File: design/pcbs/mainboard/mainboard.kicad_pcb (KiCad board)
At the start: 4 copper layers, 150 x 130 mm, 267 parts, among them J1 Conn_Coaxial, J10 Conn_01x04, J11 Conn_01x04, J15 Conn_01x01, J16 Conn_01x01, J17 Conn_01x01, J18 Conn_01x01, J2 Conn_Coaxial, J4 AudioJackSw, J5 Conn_01x03, K1 EC2-5NU, K2 EC2-5NU, K3 EC2-12NU, K4 EC2-12NU, Q1 SS8050, Q10 SS8050, Q11 SS8050, Q12 SS8050, Q13 SS8550, Q14 SS8550, Q2 SS8050, Q3 SS8050, Q4 SS8050, Q5 SS8550, Q6 SS8550, Q7 SS8050, Q8 SS8050, Q9 SS8050, U1 TPS79318-EP, U10 TPS7A49, U11 PCM1792A, U12 OPA1612AxD, U13 OPA1612AxD, U14 OPA1612AxD, U15 CCHD-575, U16 5PB1102, U17 STM8S003F3P, U18 Combo384, U19 TPS7A49, U2 SRC4392, U20 TPS7A30, U3 TLV1117-33, U4 TPS7A49, U5 TPS7A30, U6 Si8645BA-B-IU, U7 OPA1612AxD, U8 LME49600, U9 LME49600

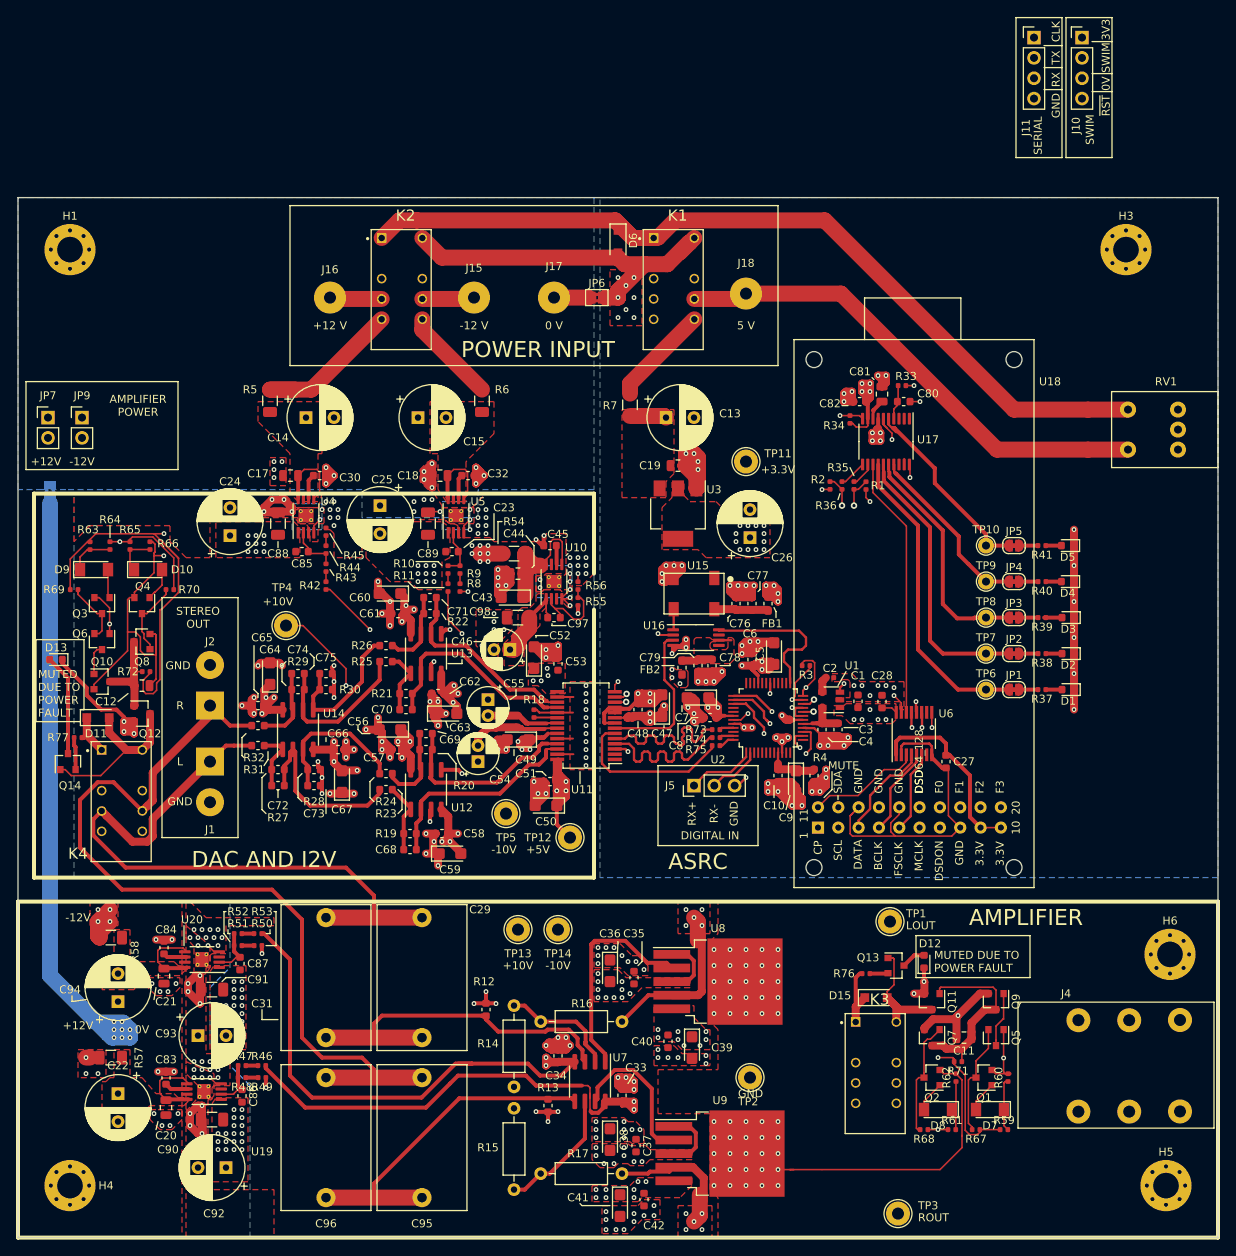
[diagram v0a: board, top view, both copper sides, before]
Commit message: Completed layout of main board, cleaned up some libraries.
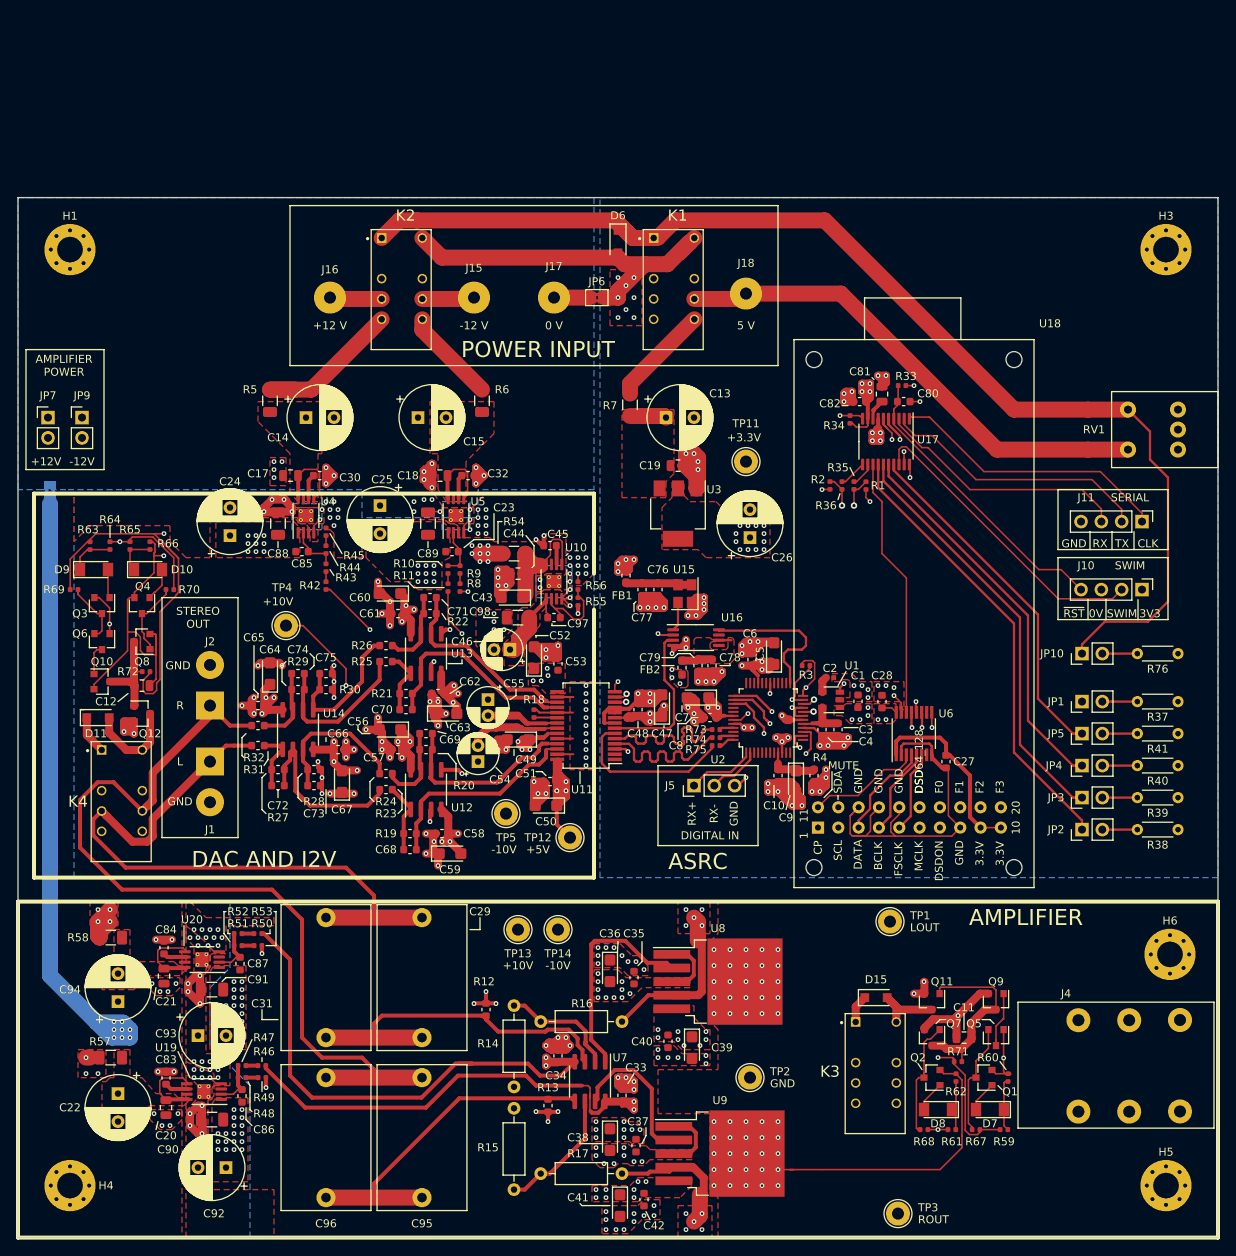
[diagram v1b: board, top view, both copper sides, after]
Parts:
- removed D1: Red, LED_SMD:LED_0603_1608Metric
- removed D12, D13: LED, LED_SMD:LED_0603_1608Metric
- removed D2: Yellow, LED_SMD:LED_0603_1608Metric
- removed D3: Green, LED_SMD:LED_0603_1608Metric
- removed D4: Blue, LED_SMD:LED_0603_1608Metric
- removed D5: White, LED_SMD:LED_0603_1608Metric
- removed Q13, Q14: SS8550, Package_TO_SOT_SMD:SOT-23
- removed R77: 1.5k, Resistor_SMD:R_0402_1005Metric
- removed TP10, TP6, TP7, TP8, TP9: ~, TestPoint:TestPoint_THTPad_D2.0mm_Drill1.0mm
- added JP10: ~, Connector_PinHeader_2.54mm:PinHeader_1x02_P2.54mm_Vertical, F.Cu at (123.0, 157.0)
- JP1, JP2, JP3, JP4, JP5: footprint Jumper:SolderJumper-2_P1.3mm_Bridged_RoundedPad1.0x1.5mm -> Connector_PinHeader_2.54mm:PinHeader_1x02_P2.54mm_Vertical
- R37, R38: value 220 -> ~; footprint Resistor_SMD:R_0402_1005Metric -> Resistor_THT:R_Axial_DIN0204_L3.6mm_D1.6mm_P5.08mm_Horizontal
- R39, R41: value 33 -> ~; footprint Resistor_SMD:R_0402_1005Metric -> Resistor_THT:R_Axial_DIN0204_L3.6mm_D1.6mm_P5.08mm_Horizontal
- R40: value 47 -> ~; footprint Resistor_SMD:R_0402_1005Metric -> Resistor_THT:R_Axial_DIN0204_L3.6mm_D1.6mm_P5.08mm_Horizontal
- R76: value 1.5k -> ~; footprint Resistor_SMD:R_0402_1005Metric -> Resistor_THT:R_Axial_DIN0204_L3.6mm_D1.6mm_P5.08mm_Horizontal
- U15: value CCHD-575 -> KC3225K24.5760C1GE00; footprint mainboard:CCHD-575 -> Crystal:Crystal_SMD_3225-4Pin_3.2x2.5mm
- moved J10 69.4 mm to (130.5, 149.0), turned to 270 degrees
- moved J11 62.0 mm to (130.5, 140.5), turned to 270 degrees
- moved R76 55.9 mm to (135.0, 157.0), turned to 180 degrees
- moved R41 29.0 mm to (135.0, 167.0)
- moved R40 28.6 mm to (135.0, 171.0)
- moved R39 28.2 mm to (135.0, 175.0)
- moved R38 27.8 mm to (135.0, 179.0)
- moved JP5 25.0 mm to (123.0, 167.0), turned to 90 degrees
- moved JP4 24.5 mm to (123.0, 171.0), turned to 90 degrees
- moved JP3 24.1 mm to (123.0, 175.0), turned to 90 degrees
- moved JP2 23.6 mm to (123.0, 179.0), turned to 90 degrees
- moved FB1 18.1 mm to (66.0, 147.2)
- moved R37 17.1 mm to (135.0, 163.0)
- moved C77 13.9 mm to (68.0, 149.0), turned to 90 degrees
- moved C76 9.91 mm to (70.0, 149.0), turned to 90 degrees
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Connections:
- JP1 pad 1: /MCU/DISP1 -> /MCU/PA1
- JP2 pad 1: /MCU/DISP2 -> /MCU/PC4
- JP3 pad 1: /MCU/DISP3 -> /MCU/PC5
- JP4 pad 1: /MCU/DISP4 -> /MCU/PC6
- JP5 pad 1: /MCU/DISP5 -> /MCU/PC7
- R37 pad 1: Net-(D1-Pad2) -> GNDD
- R38 pad 1: Net-(D2-Pad2) -> GNDD
- R39 pad 1: Net-(D3-Pad2) -> GNDD
- R40 pad 1: Net-(D4-Pad2) -> GNDD
- R41 pad 1: Net-(D5-Pad2) -> GNDD
- R76 pad 1: +10V_AMP -> GNDD
- U15 pad 1: Net-(U15-Pad1) -> GNDD
- U15 pad 2: GNDD -> Net-(C76-Pad2)
- U15 pad 3: Net-(U15-Pad3) -> Net-(C76-Pad2)
- U15 pad 4: Net-(C76-Pad2) -> Net-(U15-Pad4)
- U16 pad 1: Net-(U15-Pad3) -> Net-(U15-Pad4)
- U17 pad 14: /MCU/DISP1 -> /MCU/PC4
- U17 pad 15: /MCU/DISP2 -> /MCU/PC5
- U17 pad 16: /MCU/DISP3 -> /MCU/PC6
- U17 pad 17: /MCU/DISP4 -> /MCU/PC7
- U17 pad 5: /MCU/DISP5 -> /MCU/PA1
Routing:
- net /MCU/PC4: track 0.00 -> 56.2 mm
- net /MCU/PC5: track 0.00 -> 52.6 mm
- net /MCU/PC6: track 0.00 -> 48.3 mm
- net /MCU/PA1: track 0.00 -> 45.9 mm, vias 0 -> 1
- net /MCU/PC7: track 0.00 -> 44.1 mm
- net /PSU/POWERON: track 108.9 -> 149.1 mm
- net /MCU/DISP1: track 38.6 -> 0.00 mm
- net /MCU/SWIM: track 0.00 -> 38.2 mm
- net /MCU/DIAL: track 0.74 -> 37.0 mm, vias 0 -> 1
- net /MCU/UART_CK: track 0.00 -> 35.2 mm
- net /MCU/DISP2: track 35.0 -> 0.00 mm
- net /MCU/UART_TX: track 0.00 -> 33.8 mm
- net /MCU/NRST: track 4.36 -> 37.0 mm
- net /MCU/UART_RX: track 0.00 -> 32.0 mm
- net /MCU/DISP3: track 29.3 -> 0.00 mm
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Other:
- board text removed: "MUTED DUE TO POWER FAULT"

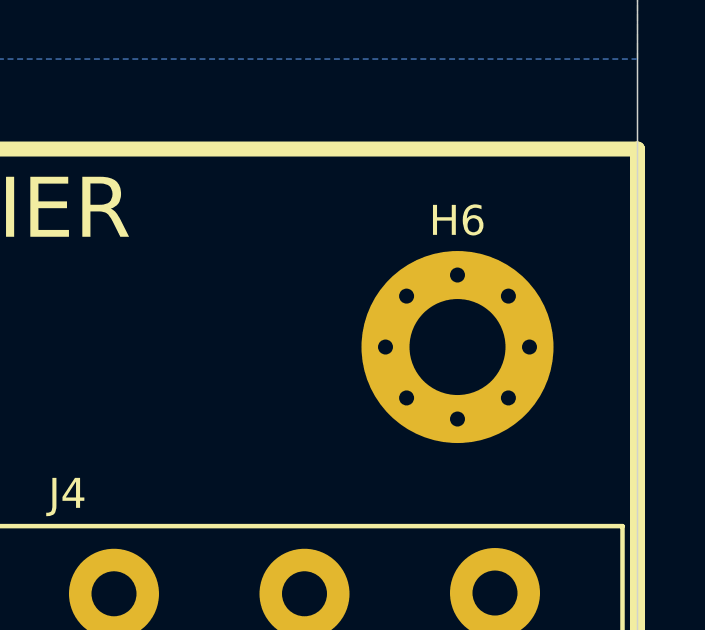
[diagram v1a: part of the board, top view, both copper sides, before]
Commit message: Fixed mounting hole alignment
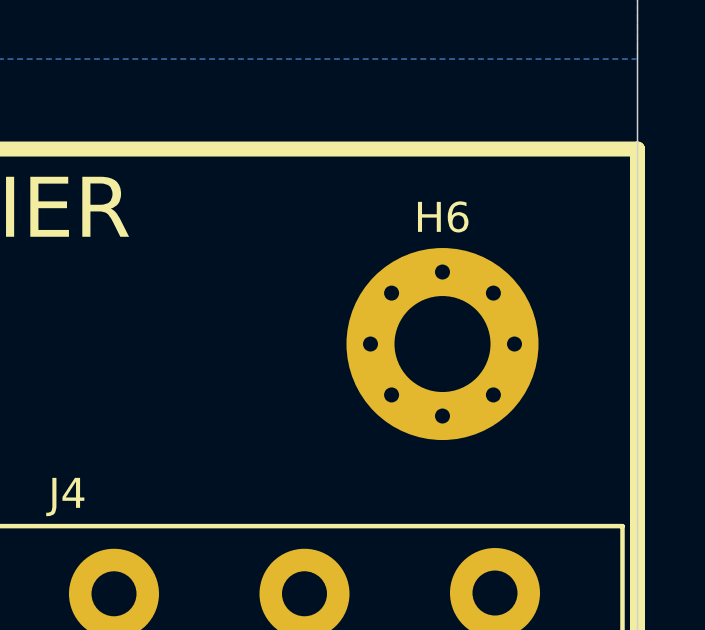
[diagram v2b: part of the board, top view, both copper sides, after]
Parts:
- moved H6 0.51 mm to (133.5, 194.5)
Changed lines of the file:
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@@
   )
   (setup
-    (last_trace_width 0.29337)
+    (last_trace_width 0.2)
     (user_trace_width 0.2)
     (user_trace_width 0.29337)
@@
   )
   (module MountingHole:MountingHole_3.2mm_M3_Pad_Via (layer F.Cu)
-    (at 134 194.6)
+    (at 133.5 194.5)
     (descr "Mounting Hole 3.2mm, M3")
     (tags "mounting hole 3.2mm m3")
@@
       (pts
         (xy 97 160.5) (xy 100.75 160.5) (xy 100.75 164) (xy 100.25 164) (xy 100.25 163)
-        (xy 97 163) (xy 97 160.5) (xy 97 160.5) (xy 97 160.5) (xy 97 160.5)
+        (xy 97 163) (xy 97 160.5)
       )
     )
@@
     (polygon
       (pts
-        (xy 99.75 165.25) (xy 99.25 165.75) (xy 97 165.75) (xy 97 163.25) (xy 97 163.25)
-        (xy 99.75 163.25)
+        (xy 99.75 165.25) (xy 99.25 165.75) (xy 97 165.75) (xy 97 163.25) (xy 99.75 163.25)
       )
     )

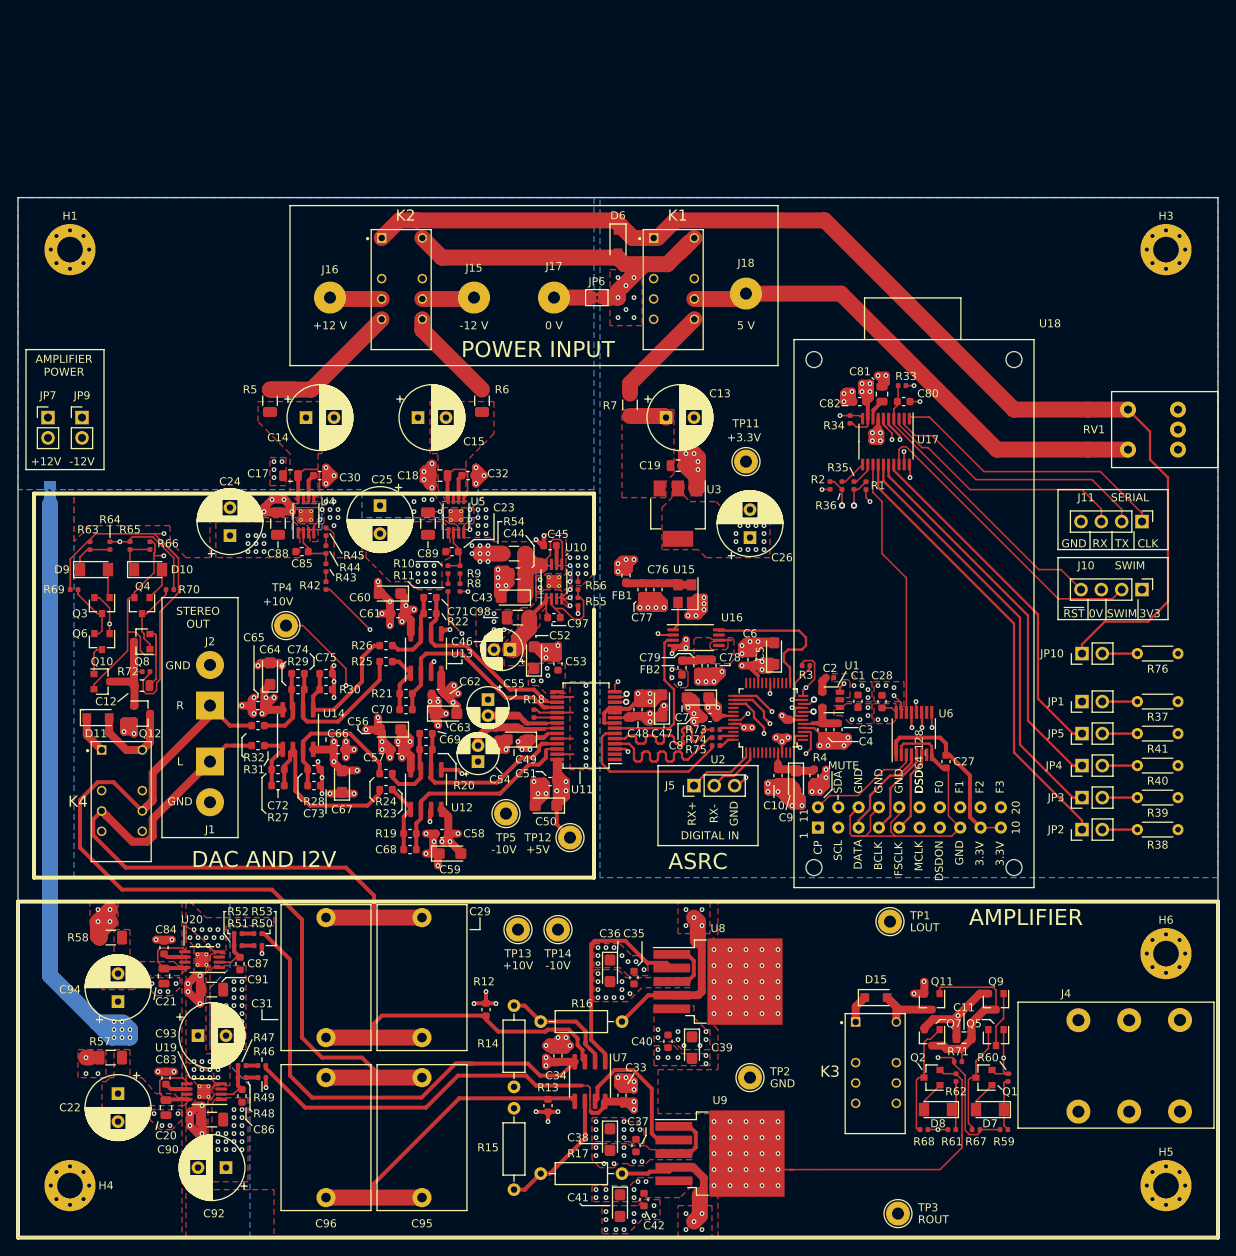
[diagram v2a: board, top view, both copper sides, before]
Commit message: Tweaked silkscreen to better identify optional modules.
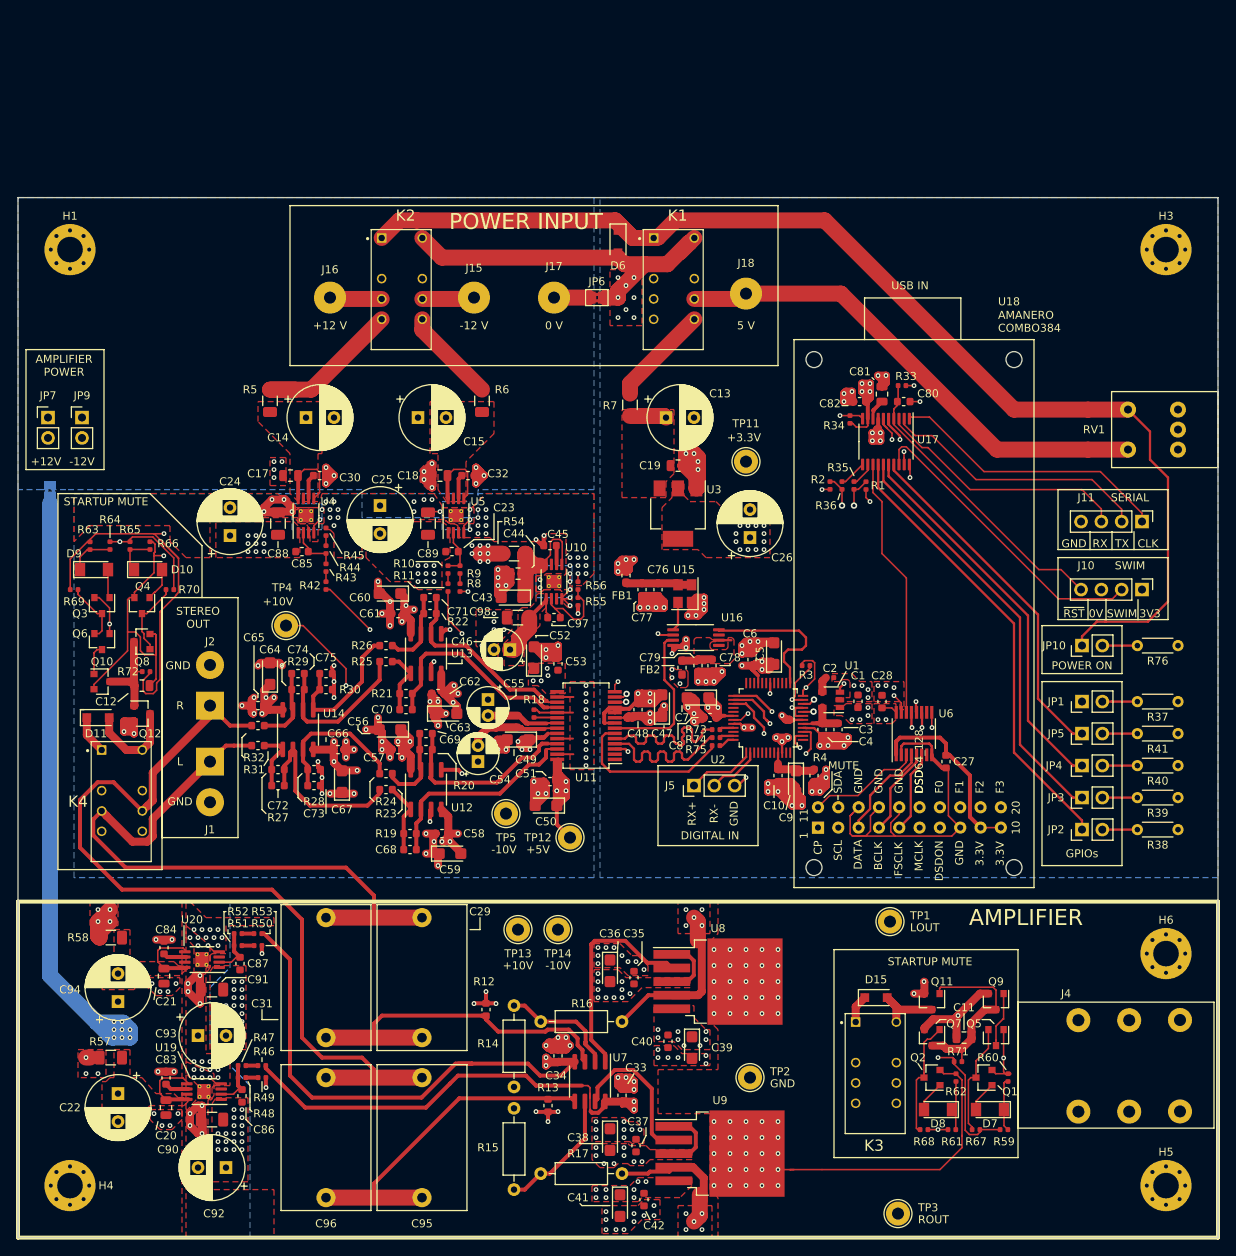
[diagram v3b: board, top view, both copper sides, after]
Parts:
- moved JP10 1.00 mm to (123.0, 156.0)
- moved R76 1.00 mm to (135.0, 156.0)
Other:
- board text added: "AMANERO COMBO384"
- board text added: "GPIOs"
- board text added: "POWER ON"
- board text added: "STARTUP MUTE"
- board text added: "USB IN"
- board text removed: "ASRC"
- board text removed: "DAC AND I2V"
